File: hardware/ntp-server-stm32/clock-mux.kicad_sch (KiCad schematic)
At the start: 10 parts, among them U52 74LVC1G157GW-Q100H, U53 74LVC1G34

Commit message: Standardize net/rail names: plain 3V3 style, _N active-low, voltage-format PG/alerts
22 net renames applied across all sheets and verified: removed/added net-name
sets match intent exactly and all node connectivity is preserved (kicad-cli
netlist re-parse).

Co-Authored-By: Claude Opus 4.8 (1M context) <noreply@anthropic.com>
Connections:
- net +3.3V renamed 3V3
- net +3.3V_CLK renamed 3V3_CLK
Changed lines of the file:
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@@
 			)
 		)
-		(property "Value" "+3.3V_CLK"
+		(property "Value" "3V3_CLK"
 			(at 147.32 77.47 0)
 			(show_name no)
@@
 			)
 		)
-		(property "Value" "+3.3V"
+		(property "Value" "3V3"
 			(at 132.08 67.31 0)
 			(show_name no)
@@
 			)
 		)
-		(property "Value" "+3.3V_CLK"
+		(property "Value" "3V3_CLK"
 			(at 201.93 78.74 0)
 			(show_name no)
@@
 			)
 		)
-		(property "Value" "+3.3V_CLK"
+		(property "Value" "3V3_CLK"
 			(at 222.25 130.81 0)
 			(show_name no)

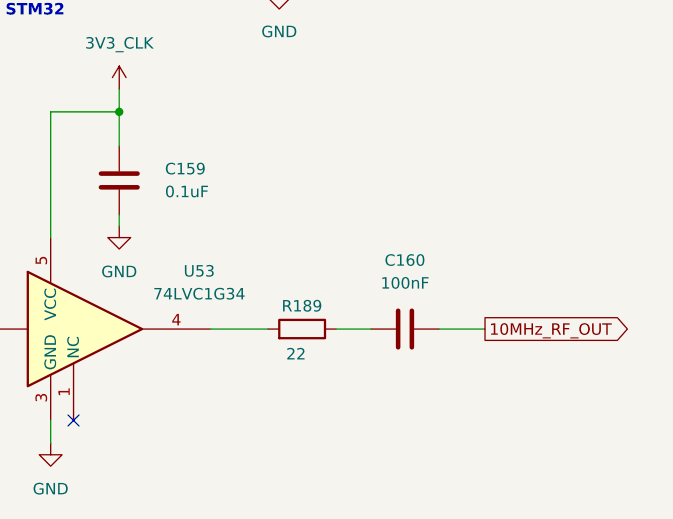
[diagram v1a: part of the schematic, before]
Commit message: Standardize + complete BOM; write fields back into KiCad symbols
- New sts1000_bom.csv: rebuilt from authoritative Value field (source MPN/footprint/
  description were corrupted by copy-paste). 338 standardized, 78 MPN-from-value,
  50 kept, ~64 flagged (SELECT/REVIEW-HV/SHUNT-REVIEW) each with full spec.
- Resistors -> deterministic Panasonic ERJ-2RKF 0402 1% 1/10W (consolidated 1 part/value).
- Caps -> verified Murata GRM parts where value matches; clean spec + footprint otherwise.
- 1633 symbol field updates (Value/Footprint/Description/MPN/Mfr/Digikey) written to
  .kicad_sch; netlist re-parse confirms connectivity byte-identical.
- Add docs/sts1000_net_naming.md naming reference.

Co-Authored-By: Claude Opus 4.8 (1M context) <noreply@anthropic.com>
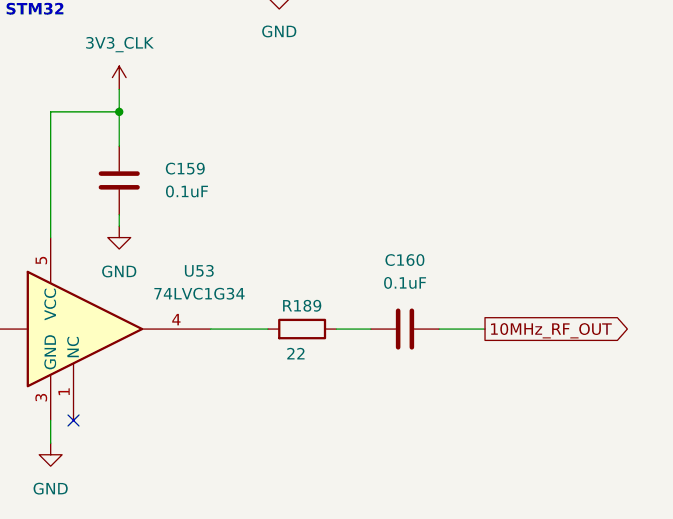
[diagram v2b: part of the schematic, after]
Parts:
- C157: footprint 0805 -> C_0603_1608Metric
- C158, C159: footprint 0805 -> C_0402_1005Metric; DIGIKEY_PART_NUMBER 445-5972-1-ND -> 490-6328-2-ND; MANUFACTURER TDK -> Murata; MANUFACTURER_PART_NUMBER C2012X7R1E475K125AB -> GRM155R71C104KA88J
- C160: value 100nF -> 0.1uF; footprint (none) -> C_0402_1005Metric; DIGIKEY_PART_NUMBER (none) -> 490-6328-2-ND; MANUFACTURER (none) -> Murata; MANUFACTURER_PART_NUMBER (none) -> GRM155R71C104KA88J
- R187, R189: footprint (none) -> R_0402_1005Metric; MANUFACTURER (none) -> Panasonic; MANUFACTURER_PART_NUMBER (none) -> ERJ-2RKF22R0X
- R188: footprint (none) -> R_0402_1005Metric; MANUFACTURER (none) -> Panasonic; MANUFACTURER_PART_NUMBER (none) -> ERJ-2RKF1003X
- U52: MANUFACTURER_PART_NUMBER (none) -> 74LVC1G157GW-Q100H
- U53: MANUFACTURER_PART_NUMBER (none) -> 74LVC1G34
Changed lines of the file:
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@@
 			)
 		)
-		(property "Footprint" ""
+		(property "Footprint" "R_0402_1005Metric"
 			(at 199.39 119.888 90)
 			(hide yes)
@@
 			)
 		)
-		(property "Description" "Resistor"
+		(property "Description" "RES SMD 22 OHM 1% 1/10W 0402"
 			(at 199.39 118.11 0)
+			(hide yes)
+			(show_name no)
+			(do_not_autoplace no)
+			(effects
+				(font
+					(size 1.27 1.27)
+				)
+			)
+		)
+		(property "MANUFACTURER" "Panasonic"
+			(at 0 0 0)
+			(hide yes)
+			(show_name no)
+			(do_not_autoplace no)
+			(effects
+				(font
+					(size 1.27 1.27)
+				)
+			)
+		)
+		(property "MANUFACTURER_PART_NUMBER" "ERJ-2RKF22R0X"
+			(at 0 0 0)
 			(hide yes)
 			(show_name no)
@@
 			)
 		)
-		(property "Value" "100nF"
+		(property "Value" "0.1uF"
 			(at 254 157.48 90)
 			(show_name no)
@@
 			)
 		)
-		(property "Footprint" ""
+		(property "Footprint" "C_0402_1005Metric"
 			(at 257.81 161.5948 0)
 			(hide yes)
@@
 			)
 		)
-		(property "Description" "Unpolarized capacitor"
+		(property "Description" "CAP CER 0.1uF 16V X7R 0402"
 			(at 254 162.56 0)
+			(hide yes)
+			(show_name no)
+			(do_not_autoplace no)
+			(effects
+				(font
+					(size 1.27 1.27)
+				)
+			)
+		)
+		(property "MANUFACTURER" "Murata"
+			(at 0 0 0)
+			(hide yes)
+			(show_name no)
+			(do_not_autoplace no)
+			(effects
+				(font
+					(size 1.27 1.27)
+				)
+			)
+		)
+		(property "MANUFACTURER_PART_NUMBER" "GRM155R71C104KA88J"
+			(at 0 0 0)
+			(hide yes)
+			(show_name no)
+			(do_not_autoplace no)
+			(effects
+				(font
+					(size 1.27 1.27)
+				)
+			)
+		)
+		(property "DIGIKEY_PART_NUMBER" "490-6328-2-ND"
+			(at 0 0 0)
 			(hide yes)
 			(show_name no)
@@
 			)
 		)
-		(property "Description" ""
+		(property "Description" "74LVC1G157GW-Q100H"
 			(at 147.32 113.03 0)
+			(hide yes)
+			(show_name no)
+			(do_not_autoplace no)
+			(effects
+				(font
+					(size 1.27 1.27)
+				)
+			)
+		)
+		(property "MANUFACTURER_PART_NUMBER" "74LVC1G157GW-Q100H"
+			(at 0 0 0)
 			(hide yes)
 			(show_name no)
@@
 			)
 		)
-		(property "Footprint" ""
+		(property "Footprint" "R_0402_1005Metric"
 			(at 242.57 164.338 90)
 			(hide yes)
@@
 			)
 		)
-		(property "Description" "Resistor"
+		(property "Description" "RES SMD 22 OHM 1% 1/10W 0402"
 			(at 242.57 162.56 0)
+			(hide yes)
+			(show_name no)
+			(do_not_autoplace no)
+			(effects
+				(font
+					(size 1.27 1.27)
+				)
+			)
+		)
+		(property "MANUFACTURER" "Panasonic"
+			(at 0 0 0)
+			(hide yes)
+			(show_name no)
+			(do_not_autoplace no)
+			(effects
+				(font
+					(size 1.27 1.27)
+				)
+			)
+		)
+		(property "MANUFACTURER_PART_NUMBER" "ERJ-2RKF22R0X"
+			(at 0 0 0)
 			(hide yes)
 			(show_name no)
@@
 			)
 		)
-		(property "Footprint" "0805"
+		(property "Footprint" "C_0603_1608Metric"
 			(at 133.0452 97.79 0)
 			(hide yes)
@@
 			)
 		)
-		(property "Description" "CAP CER 4.7UF 25V X7R 0805"
+		(property "Description" "CAP CER 1uF 16V X7R 0603"
 			(at 132.08 93.98 0)
 			(hide yes)
@@
 			)
 		)
+		(property "MANUFACTURER_PART_NUMBER" "74LVC1G34"
+			(at 0 0 0)
+			(hide yes)
+			(show_name no)
+			(do_not_autoplace no)
+			(effects
+				(font
+					(size 1.27 1.27)
+				)
+			)
+		)
 		(pin "4"
 		)
@@
 			)
 		)
-		(property "Footprint" ""
+		(property "Footprint" "R_0402_1005Metric"
 			(at 241.808 118.11 90)
 			(hide yes)
@@
 			)
 		)
-		(property "Description" "Resistor"
+		(property "Description" "RES SMD 100k OHM 1% 1/10W 0402"
 			(at 240.03 118.11 0)
+			(hide yes)
+			(show_name no)
+			(do_not_autoplace no)
+			(effects
+				(font
+					(size 1.27 1.27)
+				)
+			)
+		)
+		(property "MANUFACTURER" "Panasonic"
+			(at 0 0 0)
+			(hide yes)
+			(show_name no)
+			(do_not_autoplace no)
+			(effects
+				(font
+					(size 1.27 1.27)
+				)
+			)
+		)
+		(property "MANUFACTURER_PART_NUMBER" "ERJ-2RKF1003X"
+			(at 0 0 0)
 			(hide yes)
 			(show_name no)
@@
 			)
 		)
-		(property "Footprint" "0805"
+		(property "Footprint" "C_0402_1005Metric"
 			(at 223.2152 149.86 0)
 			(hide yes)
@@
 			)
 		)
-		(property "Description" "CAP CER 4.7UF 25V X7R 0805"
+		(property "Description" "CAP CER 0.1uF 16V X7R 0402"
 			(at 222.25 146.05 0)
 			(hide yes)
@@
 			)
 		)
-		(property "DIGIKEY_PART_NUMBER" "445-5972-1-ND"
+		(property "DIGIKEY_PART_NUMBER" "490-6328-2-ND"
 			(at 222.25 146.05 0)
 			(hide yes)
@@
 			)
 		)
-		(property "MANUFACTURER" "TDK"
+		(property "MANUFACTURER" "Murata"
 			(at 222.25 146.05 0)
 			(hide yes)
@@
 			)
 		)
-		(property "MANUFACTURER_PART_NUMBER" "C2012X7R1E475K125AB"
+		(property "MANUFACTURER_PART_NUMBER" "GRM155R71C104KA88J"
 			(at 222.25 146.05 0)
 			(hide yes)
@@
 			)
 		)
-		(property "Footprint" "0805"
+		(property "Footprint" "C_0402_1005Metric"
 			(at 202.8952 97.79 0)
 			(hide yes)
@@
 			)
 		)
-		(property "Description" "CAP CER 4.7UF 25V X7R 0805"
+		(property "Description" "CAP CER 0.1uF 16V X7R 0402"
 			(at 201.93 93.98 0)
 			(hide yes)
@@
 			)
 		)
-		(property "DIGIKEY_PART_NUMBER" "445-5972-1-ND"
+		(property "DIGIKEY_PART_NUMBER" "490-6328-2-ND"
 			(at 201.93 93.98 0)
 			(hide yes)
@@
 			)
 		)
-		(property "MANUFACTURER" "TDK"
+		(property "MANUFACTURER" "Murata"
 			(at 201.93 93.98 0)
 			(hide yes)
@@
 			)
 		)
-		(property "MANUFACTURER_PART_NUMBER" "C2012X7R1E475K125AB"
+		(property "MANUFACTURER_PART_NUMBER" "GRM155R71C104KA88J"
 			(at 201.93 93.98 0)
 			(hide yes)
